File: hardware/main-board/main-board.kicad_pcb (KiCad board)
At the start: 4 copper layers, 105 x 38 mm, 79 parts, among them J1 USB_B_Micro, J2 DNI, J3 Display Connector, J4 Conn_01x02, SW1 SW_Push, SW2 SW_Push, SW3 SW_Push, SW4 SW_Push, SW5 SW_Detect, U1 TSL2591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

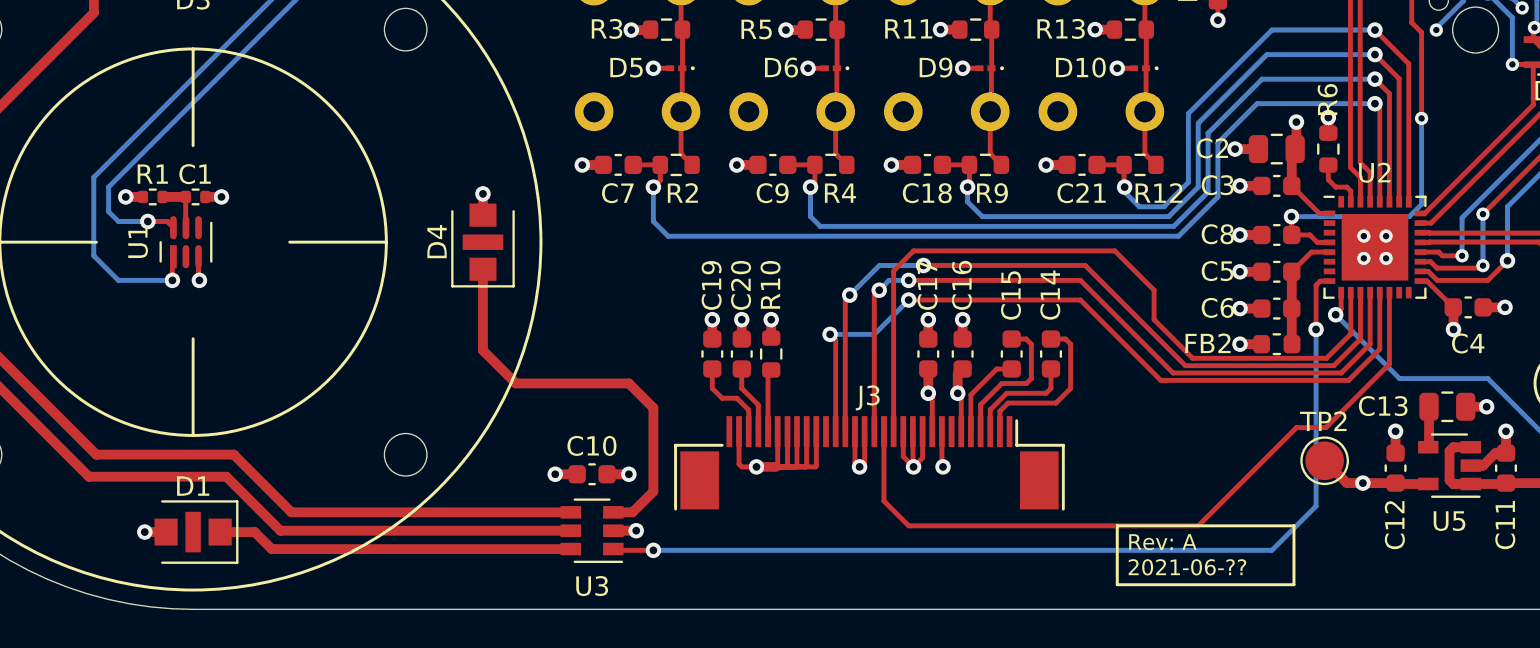
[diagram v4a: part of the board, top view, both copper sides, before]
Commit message: Moved display connector to near board edge
Also moved the display position silkscreen a bit, but the final location
is TBD pending construction of the Rev A prototype. As such, the current
3D model of the display doesn't really line up so well anymore.

The idea is that because the display needs to be raised a bit above the
PCB for improved visibility, this position change will allow for that
flexibility. Since its hard to accurately measure and remodel the
display location at this stage, and because the enclosure top is the
easiest component to tweak/recreate, its position will be measured from
the first build and fed back into the silkscreen later.
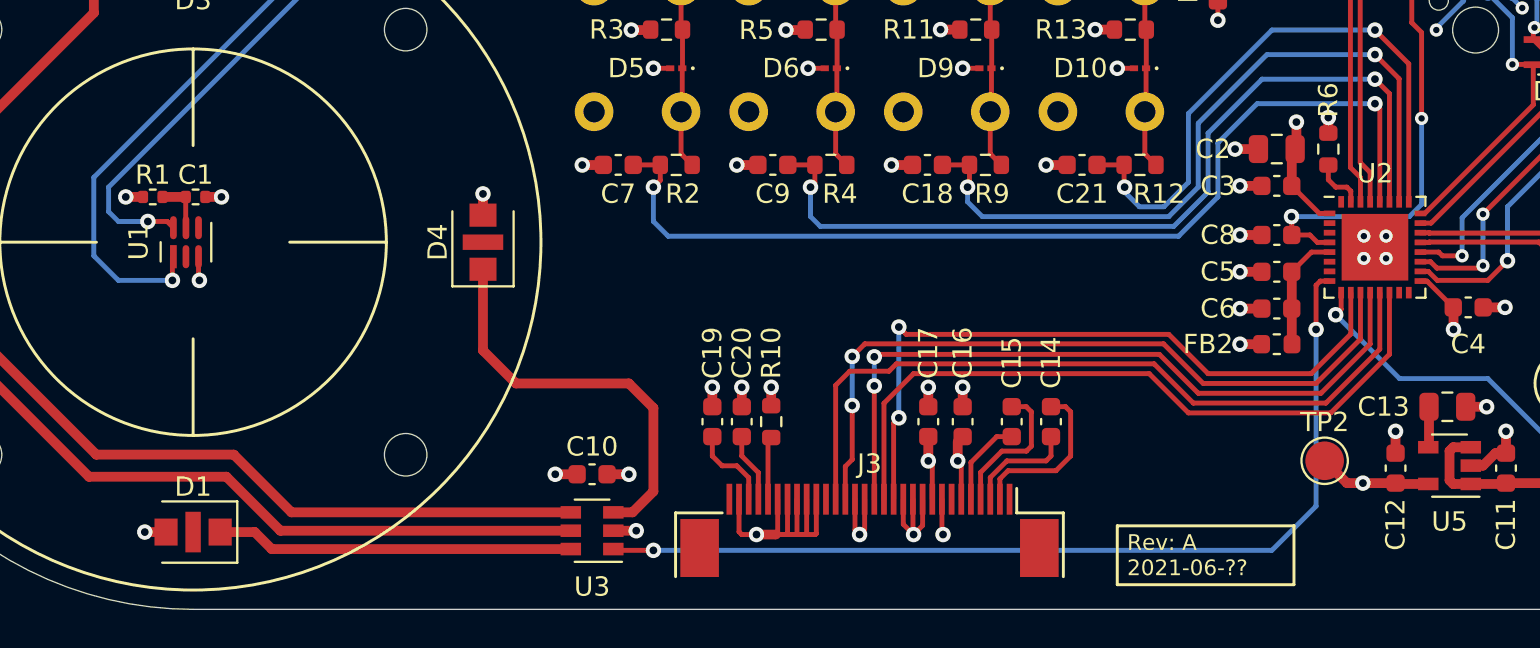
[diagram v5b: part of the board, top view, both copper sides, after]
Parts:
- moved C14 3.50 mm to (104.4, 69.3)
- moved C15 3.50 mm to (102.4, 69.3)
- moved C16 3.50 mm to (99.8, 69.3)
- moved C17 3.50 mm to (98.0, 69.3)
- moved C19 3.50 mm to (86.9, 69.3)
- moved C20 3.50 mm to (88.4, 69.3)
- moved J3 3.50 mm to (95.0, 73.5)
- moved NT2 3.50 mm to (89.7, 75.1)
- moved R10 3.50 mm to (89.9, 69.3)
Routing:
- net /DISP_~CS: track 38.3 -> 36.4 mm, vias 0 -> 2
- net /DISP_SCK: track 39.3 -> 38.3 mm
- net /DISP_D~C: track 38.3 -> 37.6 mm
- net /DISP_MOSI: track 39.6 -> 39.4 mm, vias 2 -> 0
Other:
- board text removed: "Clean up routing of display lines"

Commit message: Net tie cleanup
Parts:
- NT1: footprint NetTie:NetTie-2_SMD_Pad0.5mm -> lib_fp:NetTie-2_SMD_Pad_20mil
- NT2: footprint NetTie:NetTie-2_SMD_Pad0.5mm -> lib_fp:NetTie-2_SMD_Pad_10mil
- moved NT1 0.06 mm to (138.9, 72.5)
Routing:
- net Net-(J3-Pad21): track 14.4 -> 12.9 mm

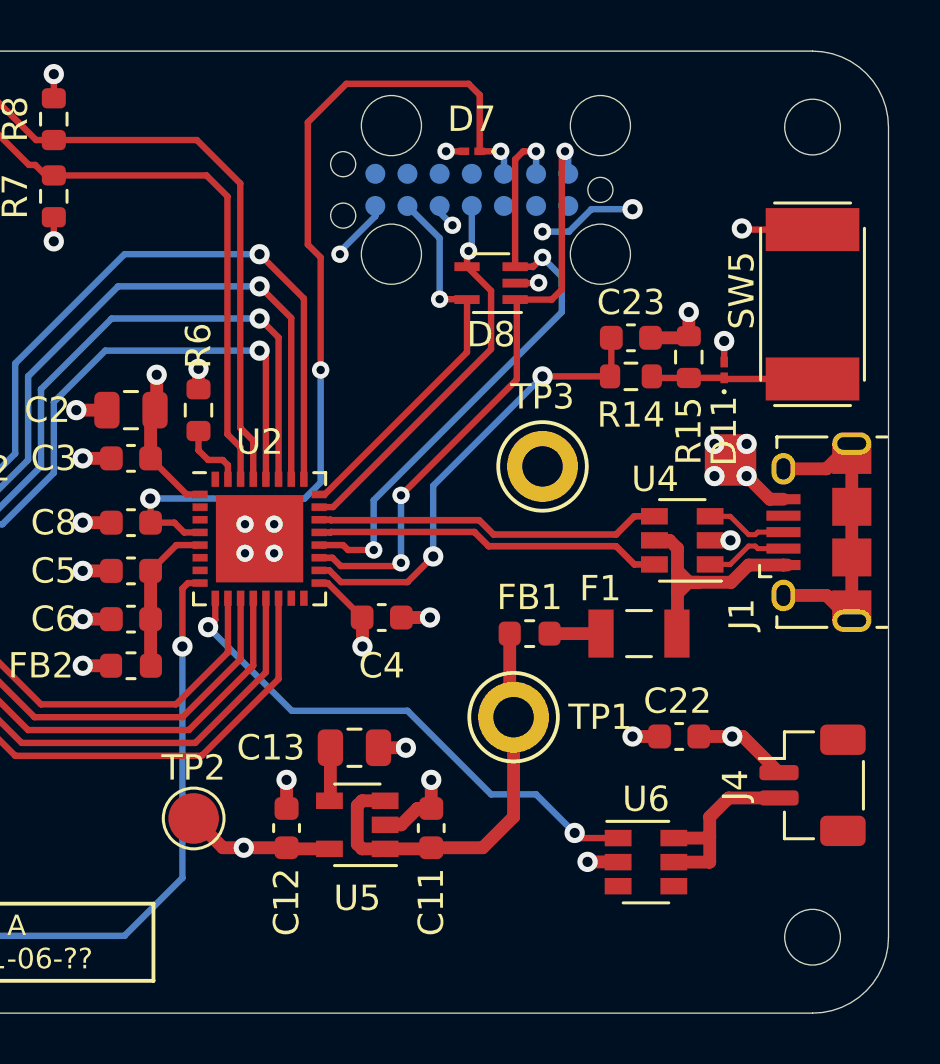
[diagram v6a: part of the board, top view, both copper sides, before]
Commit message: Test point cleanup
We don't have clearance for test point attachments on top of the PCB.
Instead, the rear screw holes will be connected to ground, and 5V for
testing will just be supplied via the USB connector like normal power.
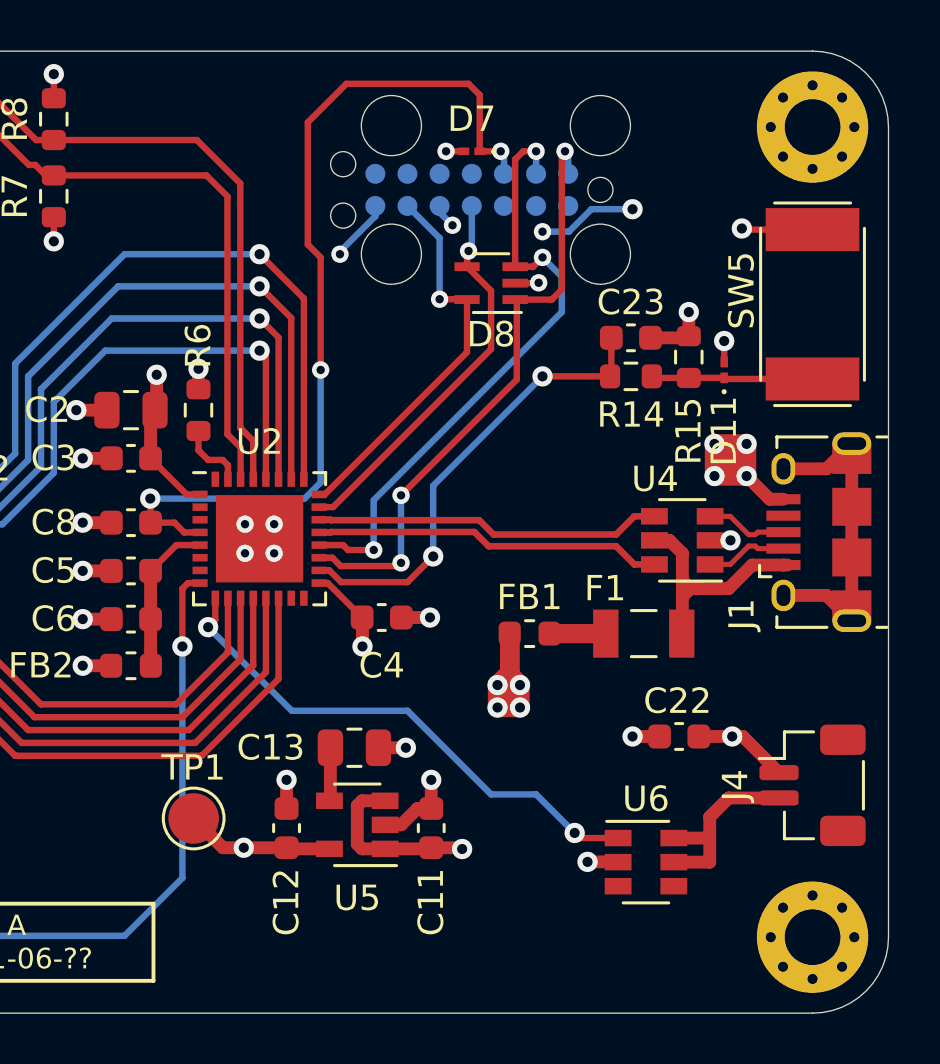
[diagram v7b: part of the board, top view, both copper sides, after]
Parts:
- removed the TP1 at (131.2, 67.3)
- removed TP3: GND, TestPoint:TestPoint_Keystone_5005-5009_Compact
- H5, H6: footprint MountingHole:MountingHole_2.2mm_M2 -> MountingHole:MountingHole_2.2mm_M2_Pad_Via
- moved F1 0.19 mm to (136.3, 64.0)
- renumbered TP2 to TP1
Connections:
- H5 pad 1: (no net) -> GND
- H6 pad 1: (no net) -> GND
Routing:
- net +5V: track 26.2 -> 26.0 mm, vias 6 -> 11

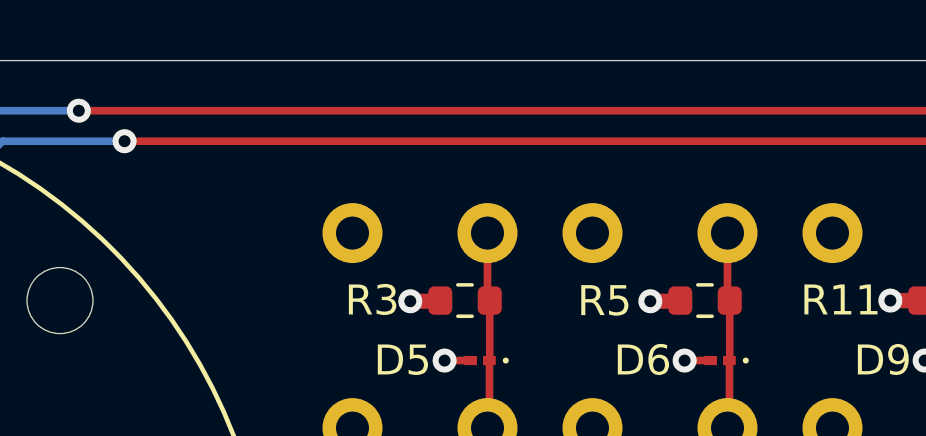
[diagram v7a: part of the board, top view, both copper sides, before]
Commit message: Various silkscreen updates
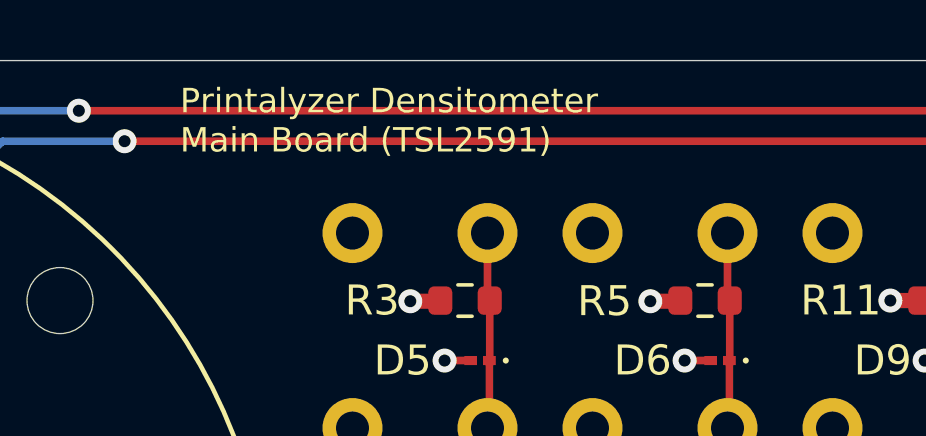
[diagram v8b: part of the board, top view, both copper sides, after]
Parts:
- added G***: LOGO, lib_fp:densitometer-logo-16_9mm, B.Cu at (124.2, 72.5)
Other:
- board text added: "Detect Switch"
- board text added: "Printalyzer Densitometer Main Board (TSL2591)"
- board text added: "Trans LED Board"
